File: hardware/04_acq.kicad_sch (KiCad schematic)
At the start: 0 parts

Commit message: init  acq board,  decided on pin maps for mcu 1,2,3  and edited esp32 symbol
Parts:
- added U5: ESP32-S3-N16R8-DEVBOARD, symbol oscil:ESP32-S3-N16R8-DEVBOARD
- added U6, U7: ADS7883, Package_TO_SOT_SMD:SOT-23-6, symbol oscil:ADS7883

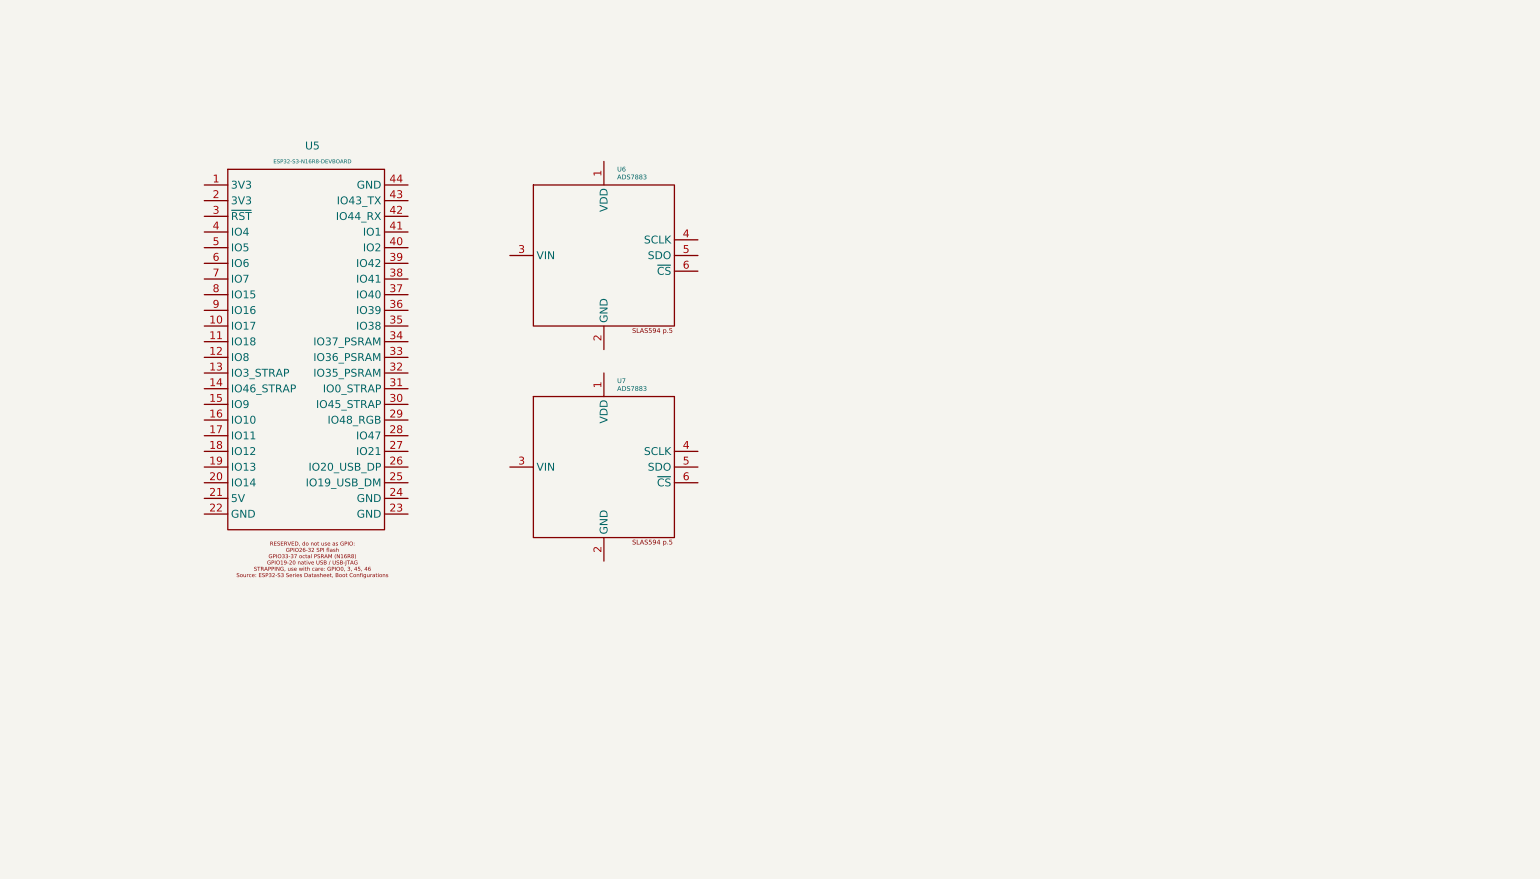
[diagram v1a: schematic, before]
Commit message: Acquisition sheet: ADC pair, module, front panel
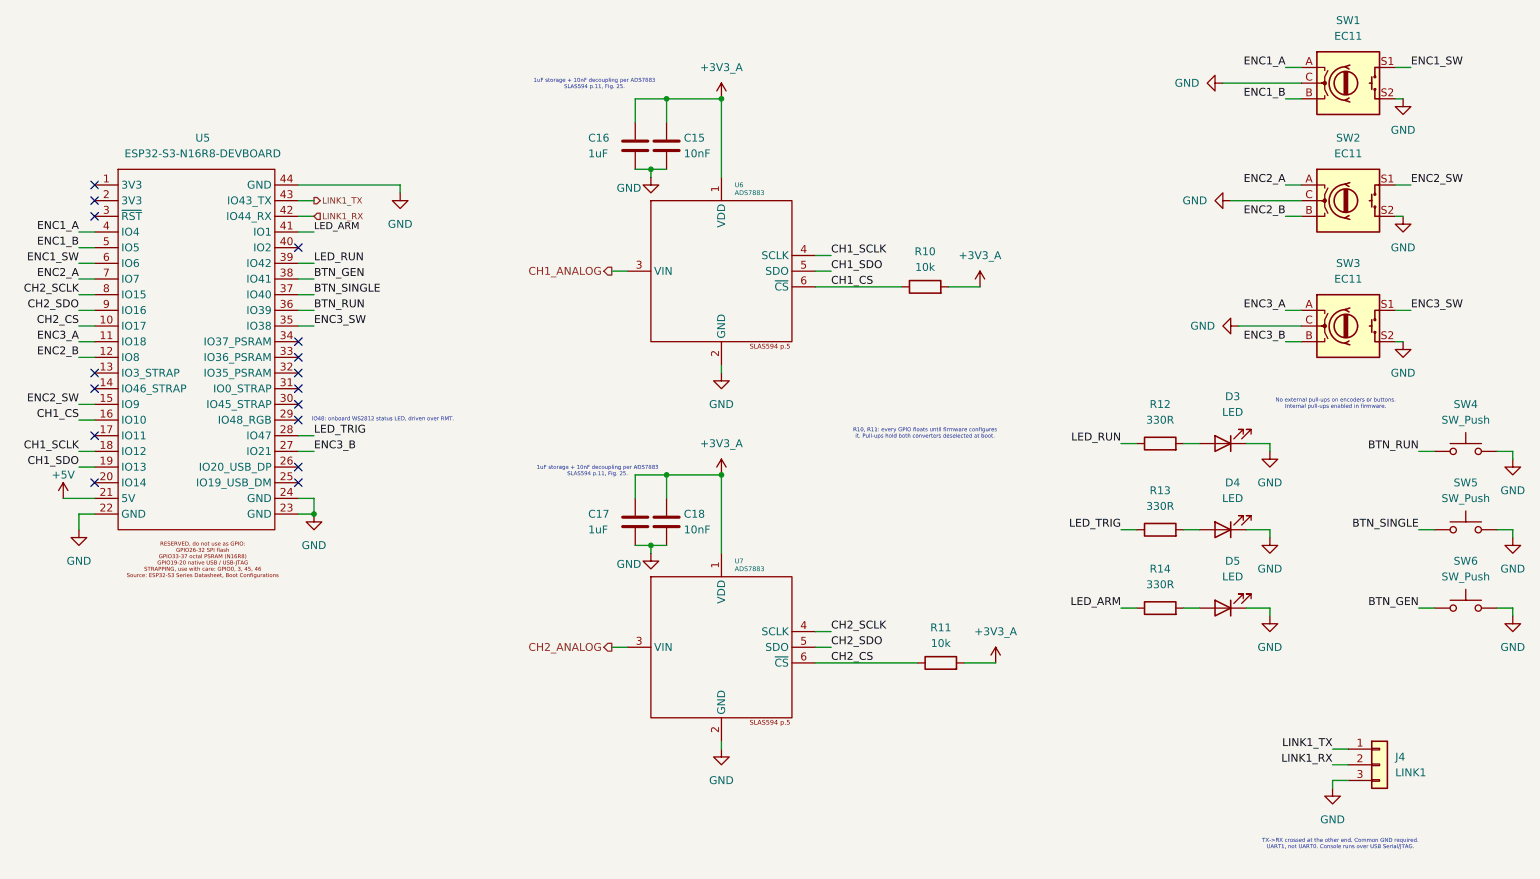
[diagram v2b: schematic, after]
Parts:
- added C15, C18: 10nF, symbol Device:C
- added C16, C17: 1uF, symbol Device:C
- added D3, D4, D5: LED, symbol Device:LED
- added J4: LINK1, symbol Connector_Generic:Conn_01x03
- added R10, R11: 10k, symbol Device:R
- added R12, R13, R14: 330R, symbol Device:R
- added SW1, SW2, SW3: EC11, symbol Device:RotaryEncoder_Switch
- added SW4, SW5, SW6: SW_Push, Button_Switch_THT:SW_NKK_GW12LJP, symbol Switch:SW_Push
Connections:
- net CH2_CS: now reaches U5.10 (IO17)
- net CH2_CS: now also U7.6 (~{CS}), R11.1
- net ENC3_A: now reaches U5.11 (IO18)
- net ENC3_A: now also SW3.A
- net ENC2_B: now reaches U5.12 (IO8)
- net ENC2_B: now also SW2.B
- net ENC2_SW: now reaches U5.15 (IO9)
- net ENC2_SW: now also SW2.S1
- net CH1_CS: now reaches U5.16 (IO10)
- net CH1_CS: now also U6.6 (~{CS}), R10.1
- net CH1_SCLK: now reaches U5.18 (IO12)
- net CH1_SCLK: now also U6.4 (SCLK)
- net CH1_SDO: now reaches U5.19 (IO13)
- net CH1_SDO: now also U6.5 (SDO)
- net +5V: now reaches U5.21 (5V)
- net GND: now reaches U5.22 (GND)
- net GND: now also U5.23 (GND), U5.24 (GND), U5.44 (GND), U6.2 (GND), U7.2 (GND), C15.2, C16.2, C17.2, C18.2, D3.1 (K), D4.1 (K), D5.1 (K), J4.3 (Pin_3), SW1.C, SW1.S2, SW2.C, SW2.S2, SW3.C, SW3.S2, SW4.2, SW5.2, SW6.2
- net ENC3_B: now reaches U5.27 (IO21)
- net ENC3_B: now also SW3.B
- net LED_TRIG: now reaches U5.28 (IO47)
- net LED_TRIG: now also R13.1
- net ENC3_SW: now reaches U5.35 (IO38)
- net ENC3_SW: now also SW3.S1
- net BTN_RUN: now reaches U5.36 (IO39)
- net BTN_RUN: now also SW4.1
- net BTN_SINGLE: now reaches U5.37 (IO40)
- net BTN_SINGLE: now also SW5.1
- net BTN_GEN: now reaches U5.38 (IO41)
- net BTN_GEN: now also SW6.1
- net LED_RUN: now reaches U5.39 (IO42)
- net LED_RUN: now also R12.1
- net ENC1_A: now reaches U5.4 (IO4)
- net ENC1_A: now also SW1.A
- net LED_ARM: now reaches U5.41 (IO1)
- net LED_ARM: now also R14.1
- net LINK1_RX: now reaches U5.42 (IO44_RX)
- net LINK1_RX: now also J4.2 (Pin_2)
- net LINK1_TX: now reaches U5.43 (IO43_TX)
- net LINK1_TX: now also J4.1 (Pin_1)
- net ENC1_B: now reaches U5.5 (IO5)
- net ENC1_B: now also SW1.B
- net ENC1_SW: now reaches U5.6 (IO6)
- net ENC1_SW: now also SW1.S1
- net ENC2_A: now reaches U5.7 (IO7)
- net ENC2_A: now also SW2.A
- net CH2_SCLK: now reaches U5.8 (IO15)
- net CH2_SCLK: now also U7.4 (SCLK)
- net CH2_SDO: now reaches U5.9 (IO16)
- net CH2_SDO: now also U7.5 (SDO)
- net +3V3_A: now reaches U7.1 (VDD)
- net +3V3_A: now also U6.1 (VDD), C15.1, C16.1, C17.1, C18.1, R10.2, R11.2
- net CH2_ANALOG: now reaches U7.3 (VIN)
- net CH1_ANALOG: now reaches U6.3 (VIN)
- new net: D5.2 (A), R14.2
- new net: D4.2 (A), R13.2
- new net: D3.2 (A), R12.2
- no-connect marks 0 -> 16
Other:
- note added: "1uF storage + 10nF decoupling per ADS7883 SLAS594 p.11, Fig. 25."
- note added: "IO48: onboard WS2812 status LED, driven over RMT."
- note added: "No external pull-ups on encoders or buttons. Internal pull-ups enabled in firmware."
- note added: "R10, R11: every GPIO floats until firmware configures it. Pull-ups hold both converters deselected at boot."
- note added: "TX->RX crossed at the other end. Common GND required. UART1, not UART0. Console runs over USB Serial/JTAG."
- moved on the sheet: U6, U7

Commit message: Add final Rev A schematic PDF and edited footprints
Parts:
- C15, C16, C17, C18: footprint (none) -> Capacitor_THT:C_Disc_D5.0mm_W2.5mm_P5.00mm
- D3, D4, D5: footprint (none) -> LED_THT:LED_D5.0mm
- J4: footprint (none) -> Connector:FanPinHeader_1x03_P2.54mm_Vertical
- R10, R11, R12, R13, R14: footprint (none) -> Resistor_THT:R_Axial_DIN0207_L6.3mm_D2.5mm_P10.16mm_Horizontal
- SW1, SW2, SW3: footprint (none) -> Rotary_Encoder:RotaryEncoder_Bourns_Horizontal_PEC09-2xxxF-Sxxxx
- SW4, SW5, SW6: footprint Button_Switch_THT:SW_NKK_GW12LJP -> Button_Switch_THT:SW_PUSH_6mm
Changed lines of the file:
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@@
 	(title_block
 		(title "Oscil")
-		(date "2026-09-18")
-		(rev "0.1")
+		(date "2026-09-21")
+		(rev "A")
 		(comment 1 "Two-channel Digital Oscilloscope and Function Generator")
 		(comment 2 "ESP32-S3 / ESP-IDF / FreeRTOS")
@@
 			)
 		)
-		(property "Footprint" ""
+		(property "Footprint" "Rotary_Encoder:RotaryEncoder_Bourns_Horizontal_PEC09-2xxxF-Sxxxx"
 			(at 231.14 61.976 0)
 			(hide yes)
@@
 			)
 		)
-		(property "Footprint" "Button_Switch_THT:SW_NKK_GW12LJP"
+		(property "Footprint" "Button_Switch_THT:SW_PUSH_6mm"
 			(at 254 93.98 0)
 			(hide yes)
@@
 			)
 		)
-		(property "Footprint" ""
+		(property "Footprint" "Resistor_THT:R_Axial_DIN0207_L6.3mm_D2.5mm_P10.16mm_Horizontal"
 			(at 166.37 61.468 90)
 			(hide yes)
@@
 			)
 		)
-		(property "Footprint" "Button_Switch_THT:SW_NKK_GW12LJP"
+		(property "Footprint" "Button_Switch_THT:SW_PUSH_6mm"
 			(at 254 106.68 0)
 			(hide yes)
@@
 			)
 		)
-		(property "Footprint" ""
+		(property "Footprint" "Resistor_THT:R_Axial_DIN0207_L6.3mm_D2.5mm_P10.16mm_Horizontal"
 			(at 204.47 113.538 90)
 			(hide yes)
@@
 			)
 		)
-		(property "Footprint" ""
+		(property "Footprint" "Capacitor_THT:C_Disc_D5.0mm_W2.5mm_P5.00mm"
 			(at 120.3452 40.64 0)
 			(hide yes)
@@
 			)
 		)
-		(property "Footprint" "Button_Switch_THT:SW_NKK_GW12LJP"
+		(property "Footprint" "Button_Switch_THT:SW_PUSH_6mm"
 			(at 254 81.28 0)
 			(hide yes)
@@
 			)
 		)
-		(property "Footprint" ""
+		(property "Footprint" "Capacitor_THT:C_Disc_D5.0mm_W2.5mm_P5.00mm"
 			(at 120.3452 101.6 0)
 			(hide yes)
@@
 			)
 		)
-		(property "Footprint" ""
+		(property "Footprint" "Connector:FanPinHeader_1x03_P2.54mm_Vertical"
 			(at 240.03 137.16 0)
 			(hide yes)
@@
 			)
 		)
-		(property "Footprint" ""
+		(property "Footprint" "LED_THT:LED_D5.0mm"
 			(at 214.63 111.76 0)
 			(hide yes)
@@
 			)
 		)
-		(property "Footprint" ""
+		(property "Footprint" "Resistor_THT:R_Axial_DIN0207_L6.3mm_D2.5mm_P10.16mm_Horizontal"
 			(at 168.91 122.428 90)
 			(hide yes)
@@
 			)
 		)
-		(property "Footprint" ""
+		(property "Footprint" "Rotary_Encoder:RotaryEncoder_Bourns_Horizontal_PEC09-2xxxF-Sxxxx"
 			(at 231.14 22.606 0)
 			(hide yes)
@@
 			)
 		)
-		(property "Footprint" ""
+		(property "Footprint" "Resistor_THT:R_Axial_DIN0207_L6.3mm_D2.5mm_P10.16mm_Horizontal"
 			(at 204.47 100.838 90)
 			(hide yes)
@@
 			)
 		)
-		(property "Footprint" ""
+		(property "Footprint" "LED_THT:LED_D5.0mm"
 			(at 214.63 99.06 0)
 			(hide yes)
@@
 			)
 		)
-		(property "Footprint" ""
+		(property "Footprint" "Rotary_Encoder:RotaryEncoder_Bourns_Horizontal_PEC09-2xxxF-Sxxxx"
 			(at 231.14 41.656 0)
 			(hide yes)
@@
 			)
 		)
-		(property "Footprint" ""
+		(property "Footprint" "Capacitor_THT:C_Disc_D5.0mm_W2.5mm_P5.00mm"
 			(at 125.4252 101.6 0)
 			(hide yes)
@@
 			)
 		)
-		(property "Footprint" ""
+		(property "Footprint" "Resistor_THT:R_Axial_DIN0207_L6.3mm_D2.5mm_P10.16mm_Horizontal"
 			(at 204.47 86.868 90)
 			(hide yes)
@@
 			)
 		)
-		(property "Footprint" ""
+		(property "Footprint" "LED_THT:LED_D5.0mm"
 			(at 214.63 85.09 0)
 			(hide yes)
@@
 			)
 		)
-		(property "Footprint" ""
+		(property "Footprint" "Capacitor_THT:C_Disc_D5.0mm_W2.5mm_P5.00mm"
 			(at 125.4252 40.64 0)
 			(hide yes)

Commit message: acq: move LED_TRIG from GPIO47 to GPIO2 so the panel LEDs sit on adjacent headers
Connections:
- net LED_TRIG: now also U5.40 (IO2); no longer U5.28 (IO47)
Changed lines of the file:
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@@
 	)
 	(no_connect
-		(at 64.77 53.34)
+		(at 64.77 83.82)
 	)
 	(no_connect
@@
 	(wire
 		(pts
-			(xy 64.77 83.82) (xy 67.31 83.82)
-		)
-		(stroke
-			(width 0)
-			(type default)
-		)
-	)
-	(wire
-		(pts
 			(xy 133.35 29.21) (xy 133.35 41.91)
 		)
@@
 		(pts
 			(xy 29.21 60.96) (xy 31.75 60.96)
+		)
+		(stroke
+			(width 0)
+			(type default)
+		)
+	)
+	(wire
+		(pts
+			(xy 64.77 53.34) (xy 67.31 53.34)
 		)
 		(stroke
@@
 		)
 	)
+	(label "LED_TRIG"
+		(at 67.31 53.34 0)
+		(effects
+			(font
+				(size 1.27 1.27)
+			)
+			(justify left bottom)
+		)
+	)
 	(label "BTN_SINGLE"
 		(at 246.38 99.06 180)
@@
 			)
 			(justify left bottom)
-		)
-	)
-	(label "LED_TRIG"
-		(at 67.31 83.82 0)
-		(effects
-			(font
-				(size 1.27 1.27)
-			)
-			(justify left bottom)

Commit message: acq: both ADCs on one SPI2 clock and CS, CH2 data to GPIO11; encoders regrouped onto headers 4-12
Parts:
- removed R11: 10k, Resistor_THT:R_Axial_DIN0207_L6.3mm_D2.5mm_P10.16mm_Horizontal, symbol Device:R
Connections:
- net CH2_SDO: now also U5.17 (IO11); no longer U5.9 (IO16)
- net ENC2_B: now also U5.8 (IO15); no longer U5.12 (IO8)
- net ENC2_SW: now also U5.9 (IO16); no longer U5.15 (IO9)
- net ENC3_A: now also U5.10 (IO17); no longer U5.11 (IO18)
- net ENC3_B: now also U5.11 (IO18); no longer U5.27 (IO21)
- net ENC3_SW: now also U5.12 (IO8); no longer U5.35 (IO38)
- net CH1_CS renamed ADC_CS
- net ADC_CS: now also U7.6 (~{CS})
- net CH1_SCLK renamed ADC_SCLK
- net ADC_SCLK: now also U7.4 (SCLK)
- removed net CH2_CS: U5.10 (IO17), U7.6 (~{CS})
- removed net CH2_SCLK: U5.8 (IO15), U7.4 (SCLK)
- no-connect marks 16 -> 18
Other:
- note added: "R10: every GPIO floats until firmware configures it. One pull-up on the shared CS holds both converters deselected at boot."
- note removed: "R10, R11: every GPIO floats until firmware configures it. Pull-ups hold both converters deselected at boot."

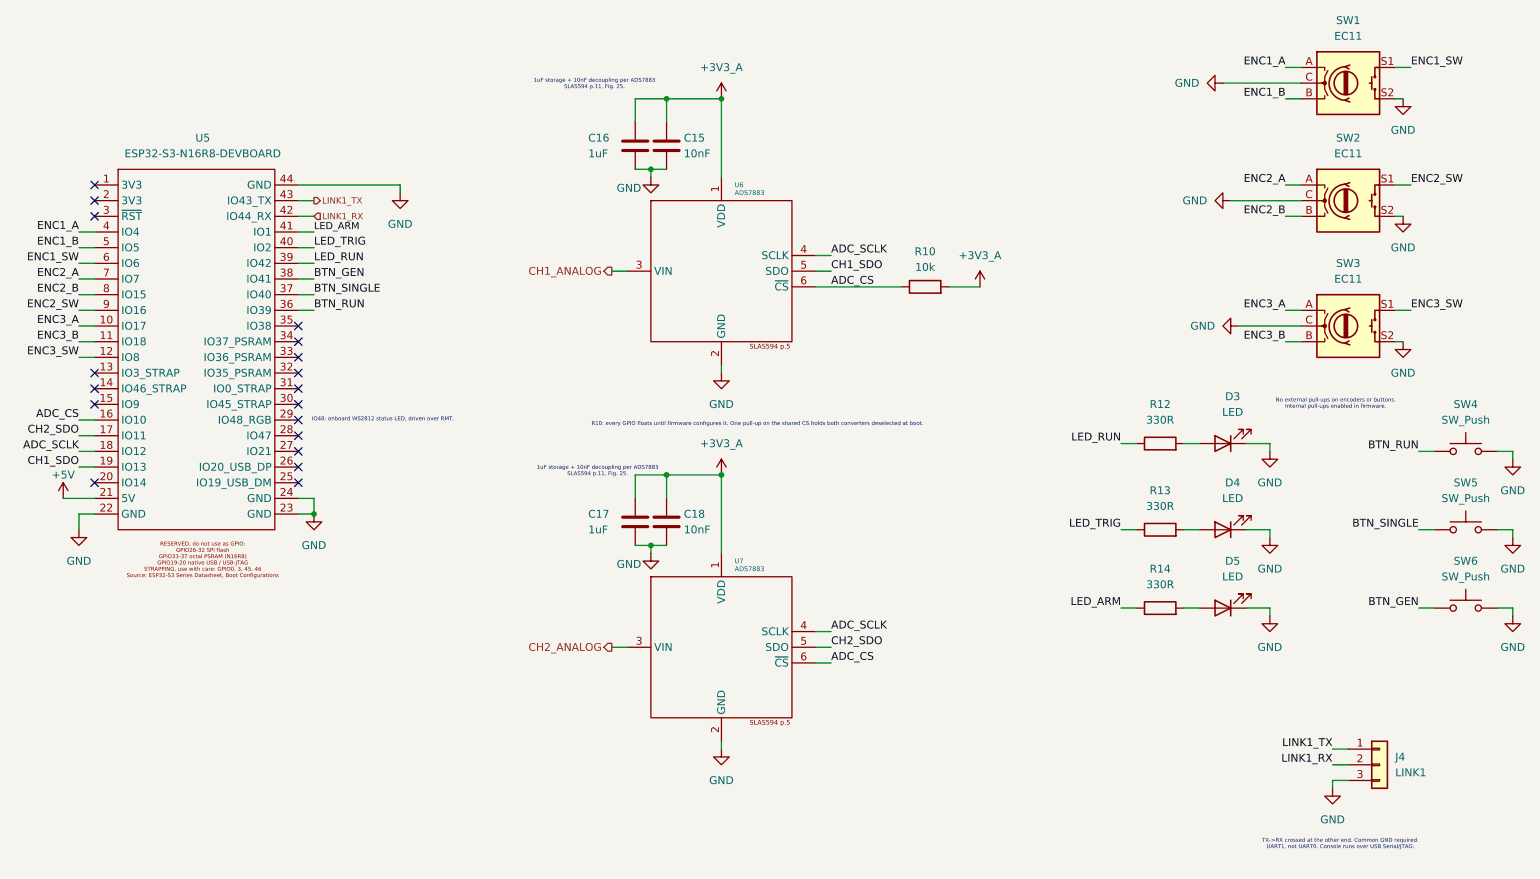
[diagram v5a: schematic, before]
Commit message: hardware: 220R series on each link line, analog decoupling notes
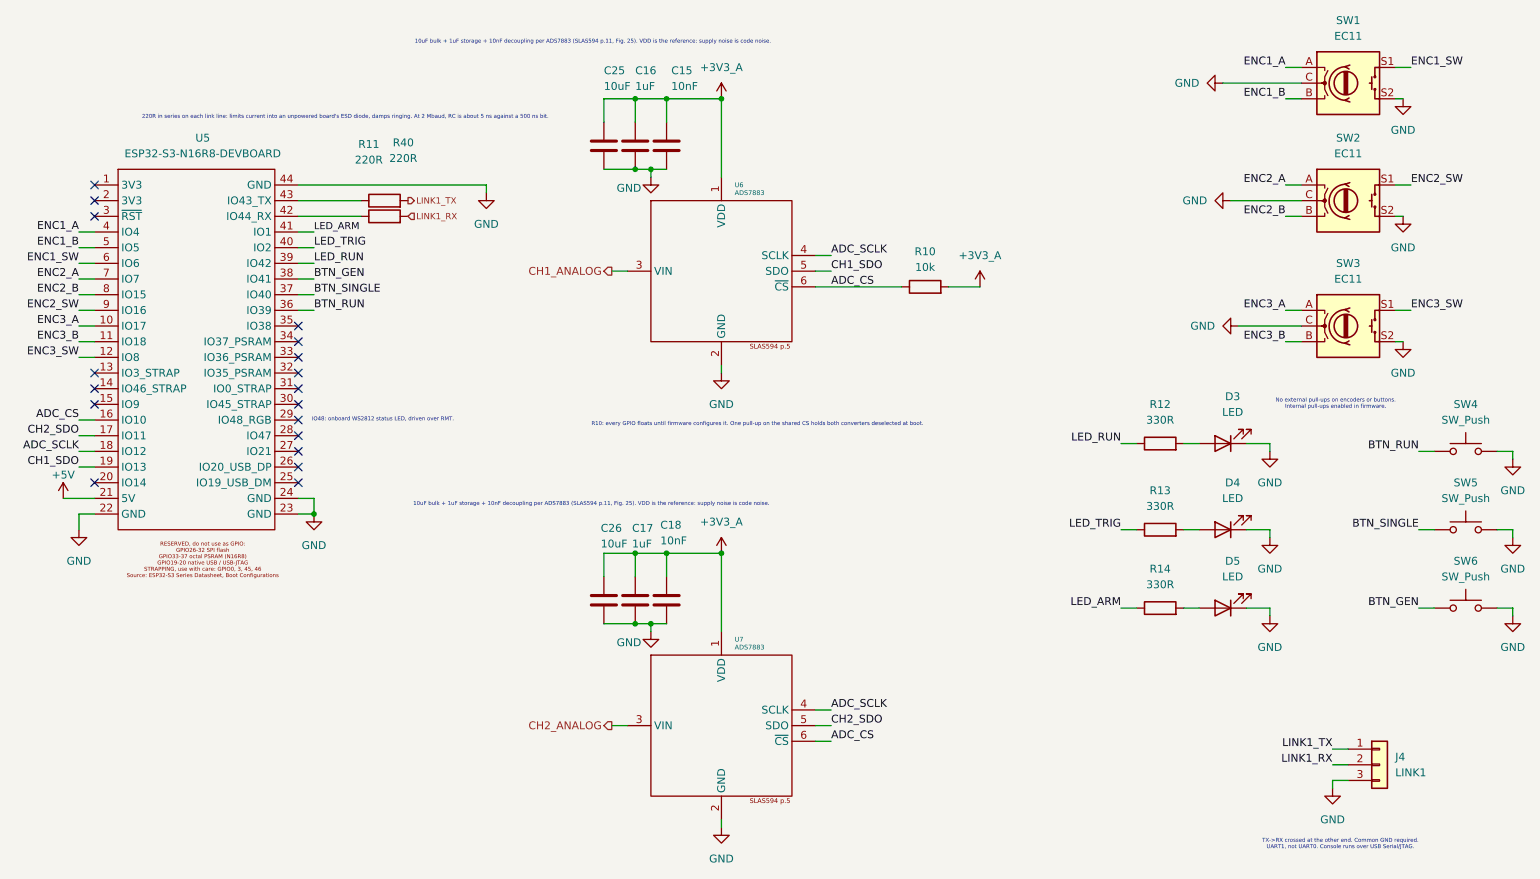
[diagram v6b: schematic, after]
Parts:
- added C25, C26: 10uF, Capacitor_THT:C_Disc_D5.0mm_W2.5mm_P5.00mm, symbol Device:C
- added R11, R40: 220R, symbol Device:R
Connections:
- net +3V3_A: now also C25.1, C26.1
- net GND: now also C25.2, C26.2
- net LINK1_RX: now also R40.2; no longer U5.42 (IO44_RX)
- net LINK1_TX: now also R11.2; no longer U5.43 (IO43_TX)
- new net: R40.1, U5.42 (IO44_RX)
- new net: R11.1, U5.43 (IO43_TX)
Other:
- note added: "10uF bulk + 1uF storage + 10nF decoupling per ADS7883 (SLAS594 p.11, Fig. 25). VDD is the reference: supply noise is code noise."
- note added: "220R in series on each link line: limits current into an unpowered board's ESD diode, damps ringing. At 2 Mbaud, RC is about 5 ns against a 500 ns bit."
- note removed: "1uF storage + 10nF decoupling per ADS7883 SLAS594 p.11, Fig. 25."
- moved on the sheet: C17, C18, U7
